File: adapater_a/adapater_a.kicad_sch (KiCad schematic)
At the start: 4 parts, among them J1 Power, J2 Digital/PWM, J3 Analog, J4 Digital/PWM

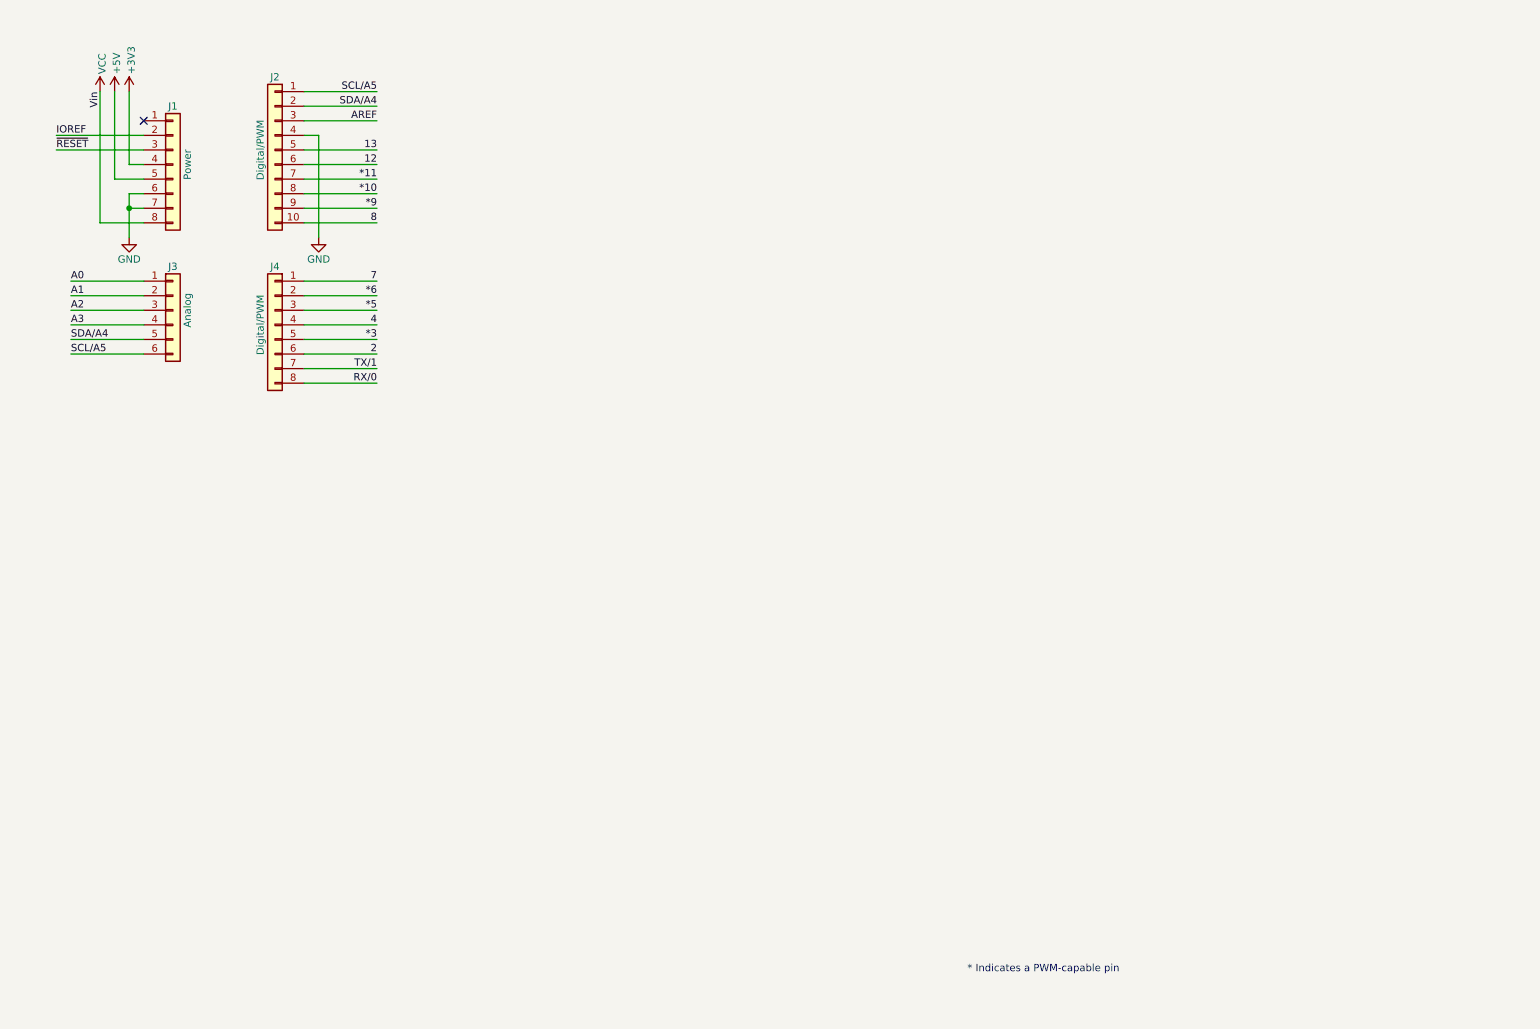
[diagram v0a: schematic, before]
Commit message: Add first version of adpater A
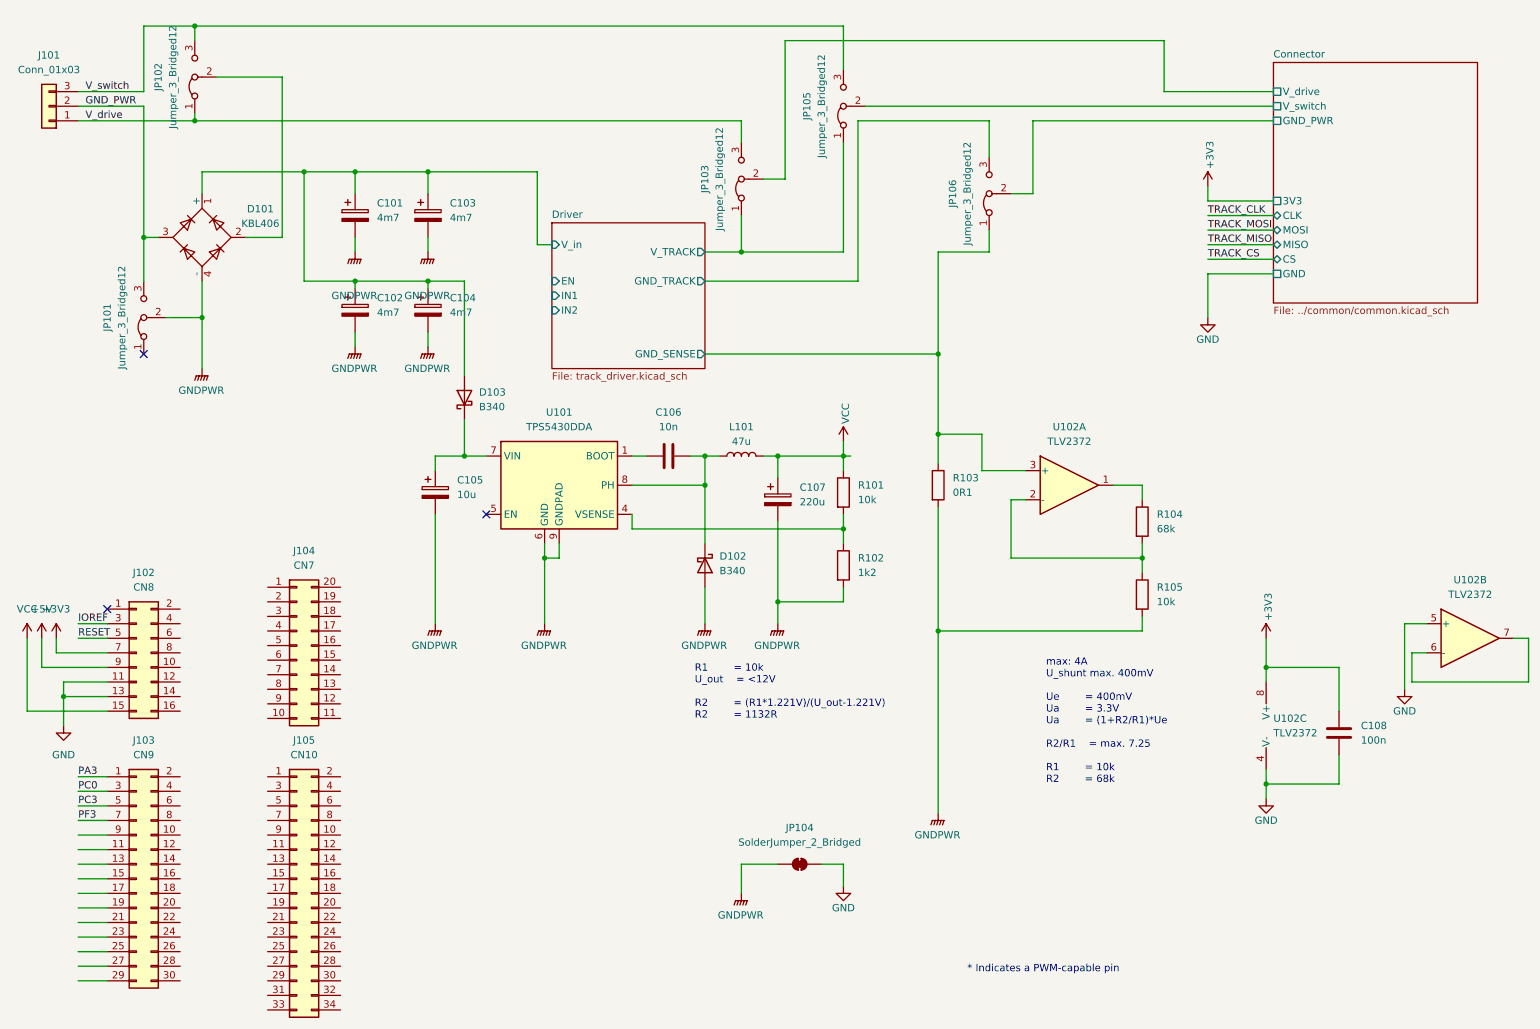
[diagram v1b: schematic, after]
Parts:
- removed J1: Power, Connector_PinSocket_2.54mm:PinSocket_1x08_P2.54mm_Vertical, symbol Connector_Generic:Conn_01x08
- removed J2: Digital/PWM, Connector_PinSocket_2.54mm:PinSocket_1x10_P2.54mm_Vertical, symbol Connector_Generic:Conn_01x10
- removed J3: Analog, Connector_PinSocket_2.54mm:PinSocket_1x06_P2.54mm_Vertical, symbol Connector_Generic:Conn_01x06
- removed J4: Digital/PWM, Connector_PinSocket_2.54mm:PinSocket_1x08_P2.54mm_Vertical, symbol Connector_Generic:Conn_01x08
- added C101, C102, C103, C104: 4m7, Capacitor_THT:CP_Radial_D18.0mm_P7.50mm, symbol Device:C_Polarized
- added C105: 10u, Capacitor_SMD:CP_Elec_6.3x5.4, symbol Device:C_Polarized
- added C106: 10n, Capacitor_SMD:C_0805_2012Metric, symbol Device:C
- added C107: 220u, Capacitor_SMD:C_Elec_10x10.2, symbol Device:C_Polarized
- added C108: 100n, Capacitor_SMD:C_0805_2012Metric, symbol Device:C
- added D101: KBL406, Diode_THT:Diode_Bridge_Vishay_KBL, symbol Diode_Bridge:GBU8M
- added D102, D103: B340, Diode_SMD:D_SMA, symbol Diode:B340
- added J101: Conn_01x03, TerminalBlock_4Ucon:TerminalBlock_4Ucon_1x03_P3.50mm_Vertical, symbol Connector_Generic:Conn_01x03
- added J102: CN8, Connector_PinHeader_2.54mm:PinHeader_2x08_P2.54mm_Vertical, symbol Connector_Generic:Conn_02x08_Odd_Even
- added J103: CN9, Connector_PinHeader_2.54mm:PinHeader_2x15_P2.54mm_Vertical, symbol Connector_Generic:Conn_02x15_Odd_Even
- added J104: CN7, Connector_PinHeader_2.54mm:PinHeader_2x10_P2.54mm_Vertical, symbol Connector_Generic:Conn_02x10_Counter_Clockwise
- added J105: CN10, Connector_PinHeader_2.54mm:PinHeader_2x17_P2.54mm_Vertical, symbol Connector_Generic:Conn_02x17_Odd_Even
- added JP101, JP102, JP103, JP105, JP106: Jumper_3_Bridged12, Connector_PinHeader_2.54mm:PinHeader_1x03_P2.54mm_Vertical, symbol Jumper:Jumper_3_Bridged12
- added JP104: SolderJumper_2_Bridged, Jumper:SolderJumper-2_P1.3mm_Bridged_RoundedPad1.0x1.5mm, symbol Jumper:SolderJumper_2_Bridged
- added L101: 47u, Inductor_SMD:L_Ferrocore_DLG-0504, symbol Device:L
- added R101, R105: 10k, Resistor_SMD:R_0805_2012Metric, symbol Device:R
- added R102: 1k2, Resistor_SMD:R_0805_2012Metric, symbol Device:R
- added R103: 0R1, Resistor_SMD:R_1206_3216Metric, symbol Device:R
- added R104: 68k, Resistor_SMD:R_0805_2012Metric, symbol Device:R
- added U101: TPS5430DDA, Package_SO:TI_SO-PowerPAD-8_ThermalVias, symbol Regulator_Switching:TPS5430DDA
- added U102: TLV2372, Package_SO:SOIC-8_3.9x4.9mm_P1.27mm, symbol Amplifier_Operational:TLV2372
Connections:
- net +3V3: now also C108.1, J102.7 (Pin_7), U102.8 (V+)
- net +5V: now also J102.9 (Pin_9)
- net GND: now also C108.2, J102.11 (Pin_11), J102.13 (Pin_13), JP104.2 (B), U102.4 (V-), U102.5 (+)
- net IOREF: now also J102.3 (Pin_3)
- net VCC: now also C107.1, J102.15 (Pin_15), L101.2, R101.1
- new net: R104.1, U102.1
- new net: R104.2, R105.1, U102.2 (-)
- new net: C106.1, U101.1 (BOOT)
- new net: R101.2, R102.1, U101.4 (VSENSE)
- new net: C105.1, D103.1 (K), U101.7 (VIN)
- new net: C106.2, D102.1 (K), L101.1, U101.8 (PH)
- new net: U102.6 (-), U102.7
- new net: D101.2, JP102.2 (C)
- new net Connector/GND_PWR: JP106.2 (C)
- new net Connector/V_drive: JP103.2 (C)
- new net Connector/V_switch: JP105.2 (C)
- new net Driver/GND_SENSE: JP106.1 (A), R103.1, U102.3 (+)
- new net Driver/GND_TRACK: JP106.3 (B)
- new net Driver/V_TRACK: JP103.1 (A), JP105.1 (A)
- new net Driver/V_in: C101.1, C102.1, C103.1, C104.1, D101.1 (+), D103.2 (A)
- new net GNDPWR: C101.2, C102.2, C103.2, C104.2, C105.2, C107.2, D101.4 (-), D102.2 (A), JP101.2 (C), JP104.1 (A), R102.2, R103.2, R105.2, U101.6 (GND), U101.9 (GNDPAD)
- new net GND_PWR: D101.3, J101.2 (Pin_2), JP101.3 (B)
- new net PA3: J103.1 (Pin_1)
- new net PC0: J103.3 (Pin_3)
- new net PC3: J103.5 (Pin_5)
- new net PF3: J103.7 (Pin_7)
- new net RESET: J102.5 (Pin_5)
- new net V_drive: J101.1 (Pin_1), JP102.1 (A), JP103.3 (B)
- new net V_switch: J101.3 (Pin_3), JP102.3 (B), JP105.3 (B)
- no-connect marks 1 -> 3
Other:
- added sheet Connector (../common/common.kicad_sch)
- added sheet Driver (track_driver.kicad_sch)
- note added: "R1 = 10k U_out = <12V R2 = (R1*1.221V)/(U_out-1.221V) R2 = 1132R"
- note added: "max: 4A U_shunt max. 400mV Ue = 400mV Ua = 3.3V Ua = (1+R2/R1)*Ue R2/R1 = max. 7.25 R1 = 10k R2 = 68k"
